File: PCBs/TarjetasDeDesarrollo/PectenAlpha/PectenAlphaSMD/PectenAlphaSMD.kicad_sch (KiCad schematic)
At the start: 28 parts, among them J1 ICSP, J2 GPIO, J3 USB_A, Q1 PN2222A, SW1 SW_Push, SW2 SW_DIP_x04, U1 PIC_8-14-18-20, U2 D148K, U3 CH340N

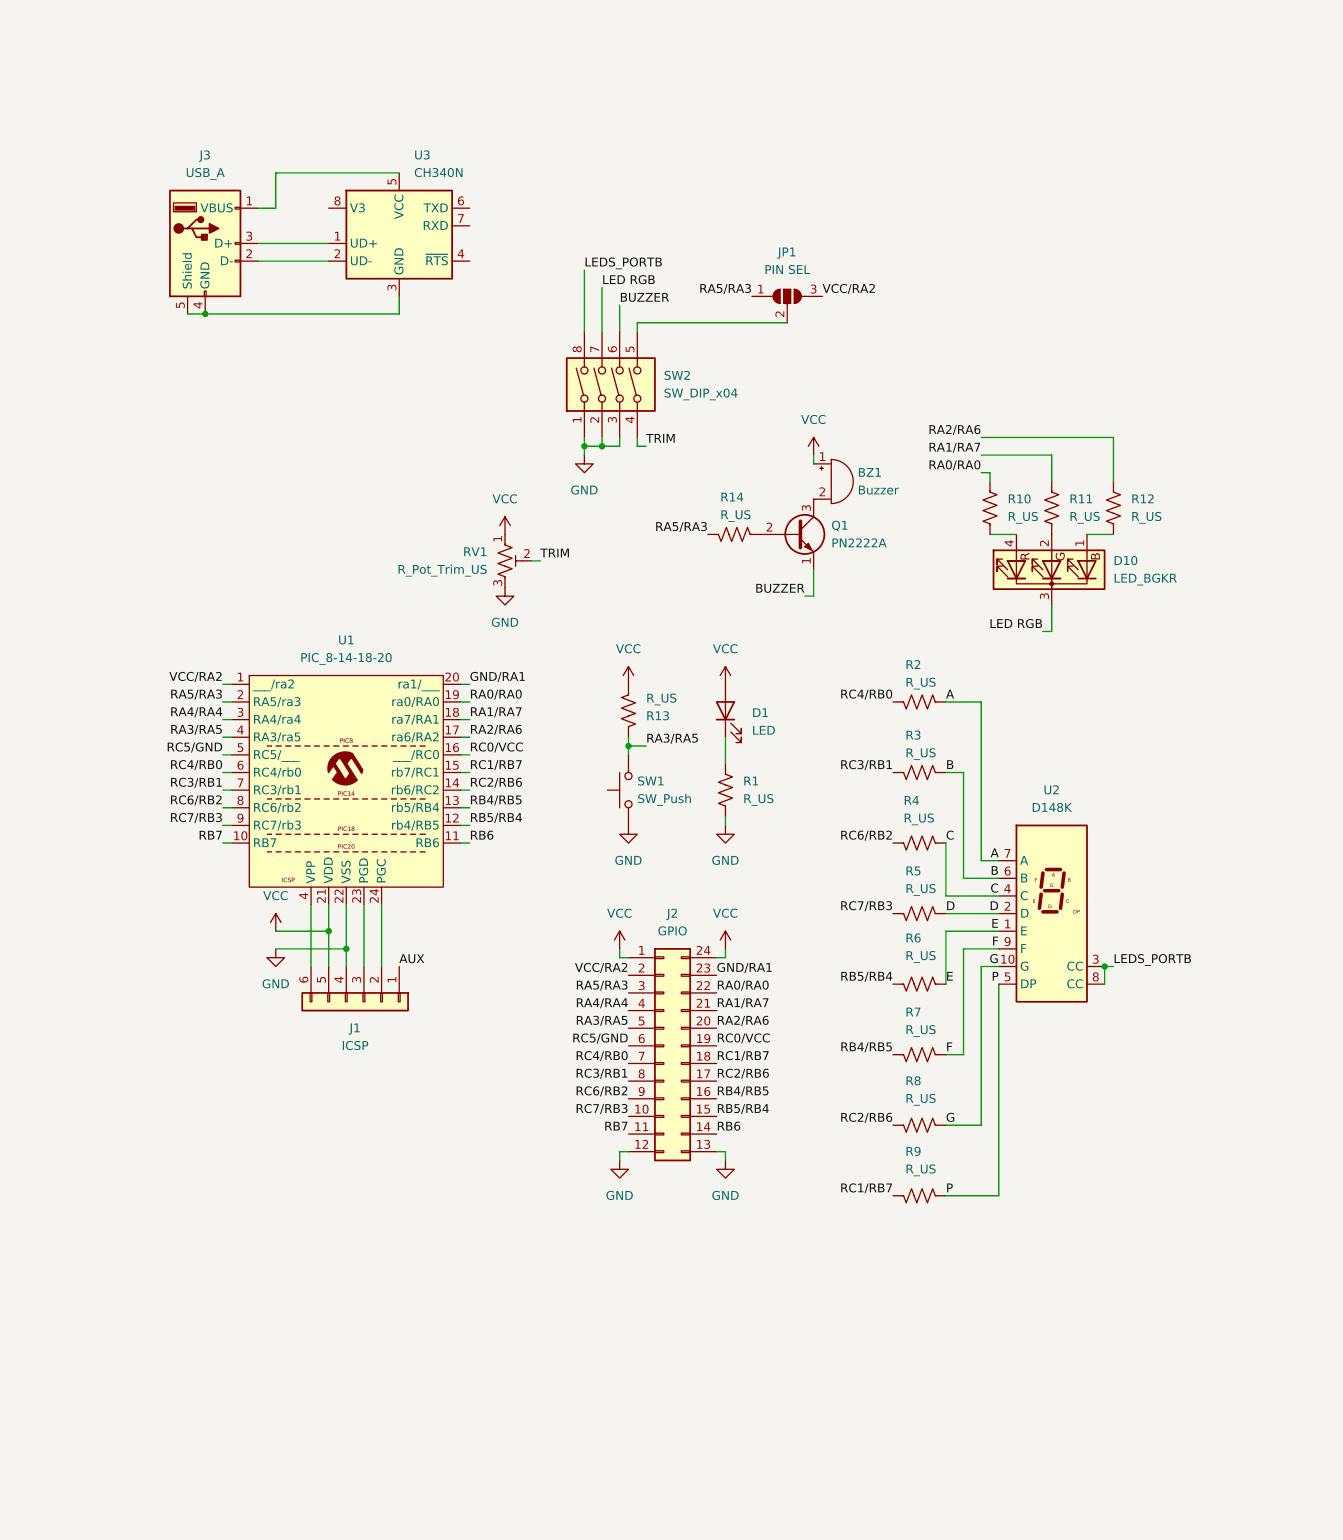
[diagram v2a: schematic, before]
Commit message: Se inició una importante modificación de la tarjeta pectenAlpha
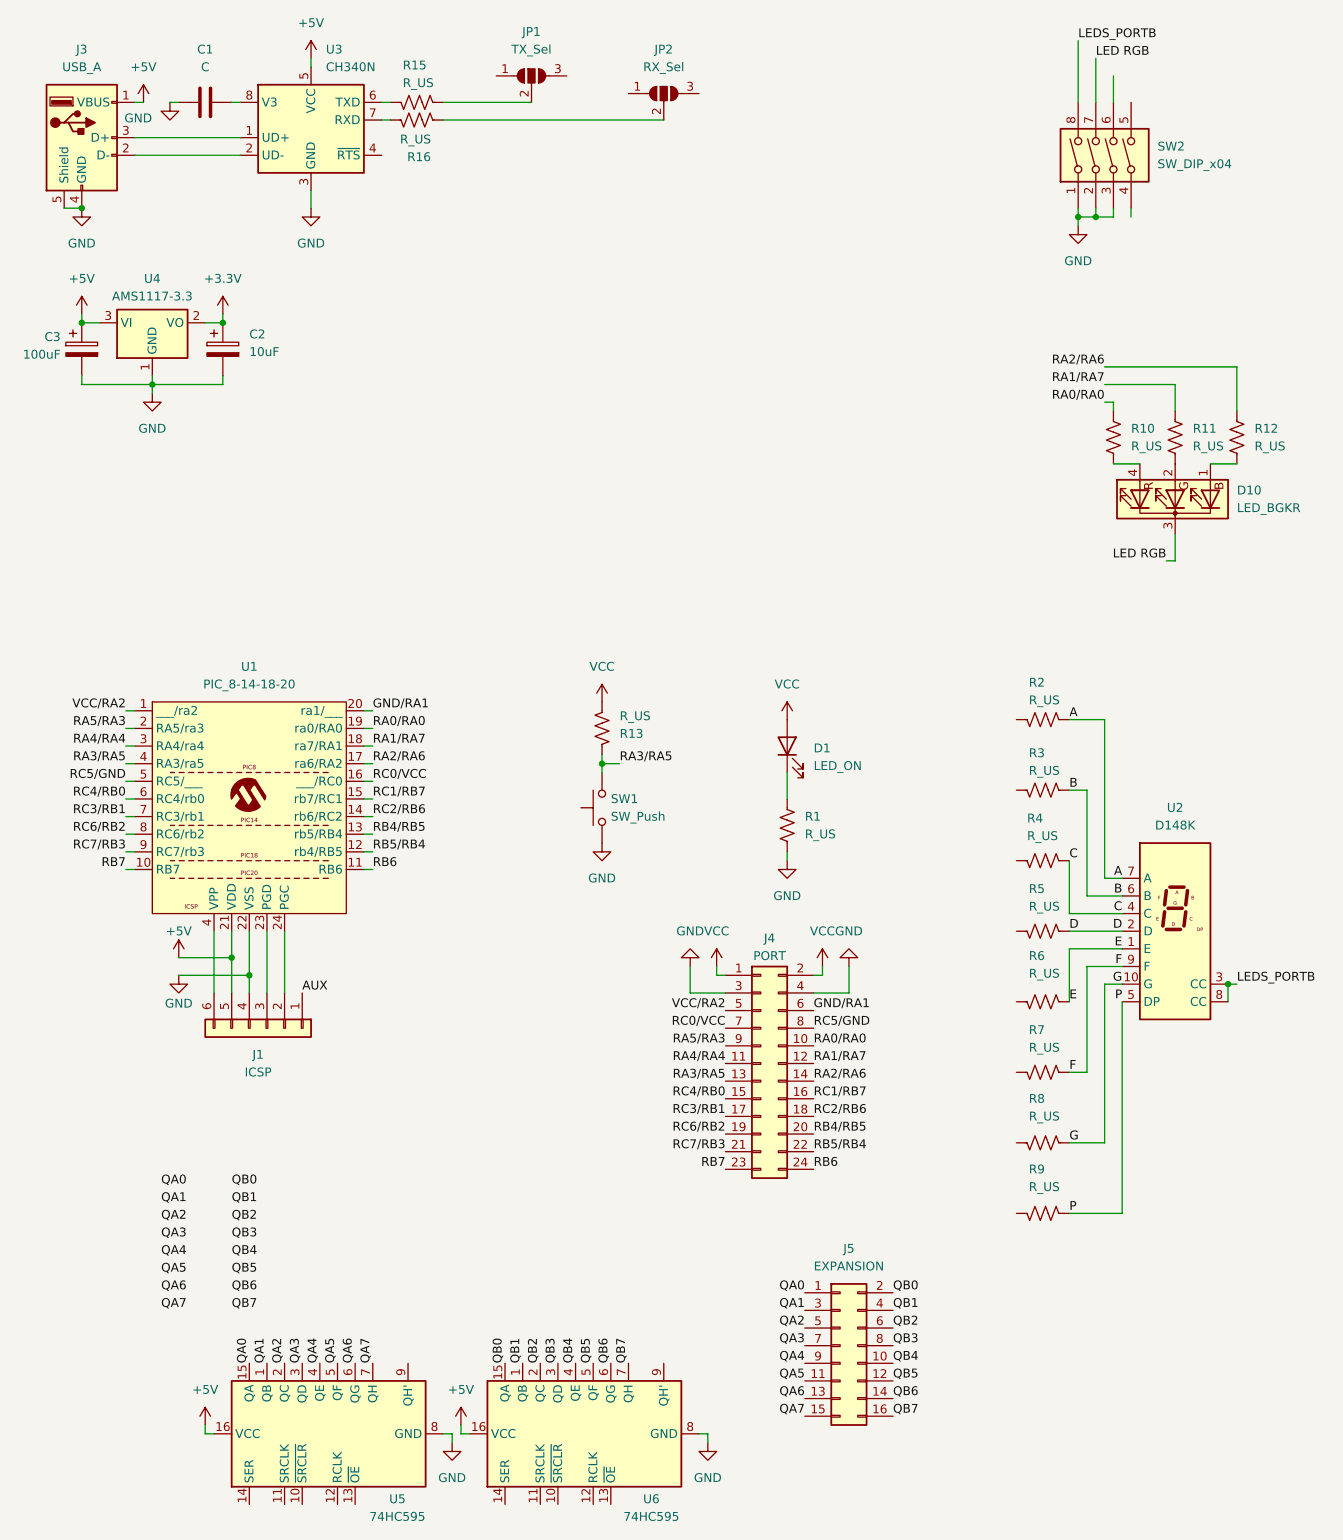
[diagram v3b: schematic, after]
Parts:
- removed BZ1: Buzzer, Buzzer_Beeper:Buzzer_12x9.5RM7.6, symbol Device:Buzzer
- removed J2: GPIO, Connector_PinHeader_2.54mm:PinHeader_2x12_P2.54mm_Vertical, symbol Connector_Generic:Conn_02x12_Counter_Clockwise
- removed Q1: PN2222A, Package_TO_SOT_THT:TO-92L_HandSolder, symbol Transistor_BJT:PN2222A
- removed R14: R_US, Resistor_SMD:R_0805_2012Metric_Pad1.20x1.40mm_HandSolder, symbol Device:R_US
- removed RV1: R_Pot_Trim_US, Potentiometer_THT:Potentiometer_Runtron_RM-065_Vertical, symbol Device:R_Potentiometer_Trim_US
- added C1: C, symbol Device:C
- added C2: 10uF, symbol Device:C_Polarized
- added C3: 100uF, symbol Device:C_Polarized
- added J4: PORT, Connector_PinHeader_2.54mm:PinHeader_2x12_P2.54mm_Vertical, symbol Connector_Generic:Conn_02x12_Odd_Even
- added J5: EXPANSION, Connector_PinHeader_2.54mm:PinHeader_2x08_P2.54mm_Vertical, symbol Connector_Generic:Conn_02x08_Odd_Even
- added JP2: RX_Sel, symbol Jumper:SolderJumper_3_Open
- added R15, R16: R_US, Resistor_SMD:R_0805_2012Metric_Pad1.20x1.40mm_HandSolder, symbol Device:R_US
- added U4: AMS1117-3.3, Package_TO_SOT_SMD:SOT-223-3_TabPin2, symbol Regulator_Linear:AMS1117-3.3
- added U5, U6: 74HC595, symbol 74xx:74HC595
- D1: value LED -> LED_ON
- JP1: value PIN SEL -> TX_Sel; footprint Jumper:SolderJumper-3_P1.3mm_Open_RoundedPad1.0x1.5mm -> (none)
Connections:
- net GND: now also J3.4 (GND), J3.5 (Shield), U3.3 (GND), C1.1, C2.2, C3.2, J4.3 (Pin_3), J4.4 (Pin_4), U4.1 (GND), U5.8 (GND), U6.8 (GND)
- net GND/RA1: now also J4.6 (Pin_6)
- net RA0/RA0: now also J4.10 (Pin_10)
- net RA1/RA7: now also J4.12 (Pin_12)
- net RA2/RA6: now also J4.14 (Pin_14)
- net RA3/RA5: now also J4.13 (Pin_13)
- net RA4/RA4: now also J4.11 (Pin_11)
- net RA5/RA3: now also J4.9 (Pin_9); no longer JP1.1 (A)
- net RB4/RB5: now also J4.20 (Pin_20); no longer R7.1
- net RB5/RB4: now also J4.22 (Pin_22); no longer R6.1
- net RB6: now also J4.24 (Pin_24)
- net RB7: now also J4.23 (Pin_23)
- net RC0/VCC: now also J4.7 (Pin_7)
- net RC1/RB7: now also J4.16 (Pin_16); no longer R9.1
- net RC2/RB6: now also J4.18 (Pin_18); no longer R8.1
- net RC3/RB1: now also J4.17 (Pin_17); no longer R3.1
- net RC4/RB0: now also J4.15 (Pin_15); no longer R2.1
- net RC5/GND: now also J4.8 (Pin_8)
- net RC6/RB2: now also J4.19 (Pin_19); no longer R4.1
- net RC7/RB3: now also J4.21 (Pin_21); no longer R5.1
- net VCC: now also J4.1 (Pin_1), J4.2 (Pin_2); no longer J1.5 (Pin_5), U1.21 (VDD)
- net VCC/RA2: now also J4.5 (Pin_5); no longer JP1.3 (B)
- net at JP1.2 (C): now also R15.1; no longer SW2.5
- net +5V: now reaches J3.1 (VBUS), U3.5 (VCC)
- net +5V: now also J1.5 (Pin_5), U1.21 (VDD), C3.1, U4.3 (VI), U5.16 (VCC), U6.16 (VCC)
- net at U3.6 (TXD): now also R15.2
- net at U3.7 (RXD): now also R16.1
- net at U3.8 (V3): now also C1.2
- net BUZZER: no longer names the net of SW2.6
- net TRIM: no longer names the net of SW2.4
- new net: JP2.2 (C), R16.2
- new net +3.3V: C2.1, U4.2 (VO)
- new net QA0: J5.1 (Pin_1), U5.15 (QA)
- new net QA1: J5.3 (Pin_3), U5.1 (QB)
- new net QA2: J5.5 (Pin_5), U5.2 (QC)
- new net QA3: J5.7 (Pin_7), U5.3 (QD)
- new net QA4: J5.9 (Pin_9), U5.4 (QE)
- new net QA5: J5.11 (Pin_11), U5.5 (QF)
- new net QA6: J5.13 (Pin_13), U5.6 (QG)
- new net QA7: J5.15 (Pin_15), U5.7 (QH)
- new net QB0: J5.2 (Pin_2), U6.15 (QA)
- new net QB1: J5.4 (Pin_4), U6.1 (QB)
- new net QB2: J5.6 (Pin_6), U6.2 (QC)
- new net QB3: J5.8 (Pin_8), U6.3 (QD)
- new net QB4: J5.10 (Pin_10), U6.4 (QE)
- new net QB5: J5.12 (Pin_12), U6.5 (QF)
- new net QB6: J5.14 (Pin_14), U6.6 (QG)
- new net QB7: J5.16 (Pin_16), U6.7 (QH)
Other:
- moved on the sheet: D1, D10, J1, J3, R1, R10, R11, R12, R13, R2, R3, R4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
